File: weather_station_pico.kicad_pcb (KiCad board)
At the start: 2 copper layers, 60.2 x 74.1 mm, 24 parts, among them J1 UART_DEBUG, J2 1984617, J3 STEMMA, J4 STEMMA_QT, J5 DS18B20, J6 1X7_HEADER, J7 RJ11, J8 RJ11, U1 PICO_W, U2 BME280

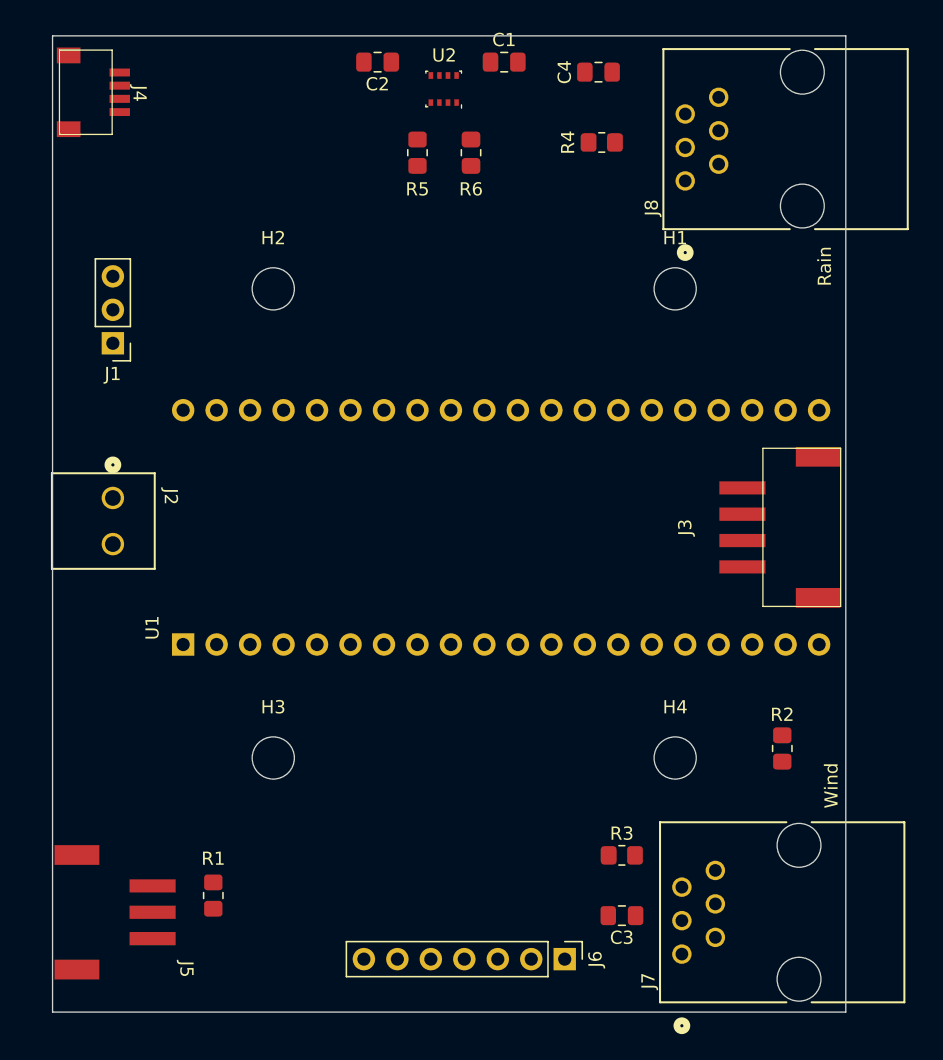
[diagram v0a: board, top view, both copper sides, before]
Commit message: Added footprints for antenna connector
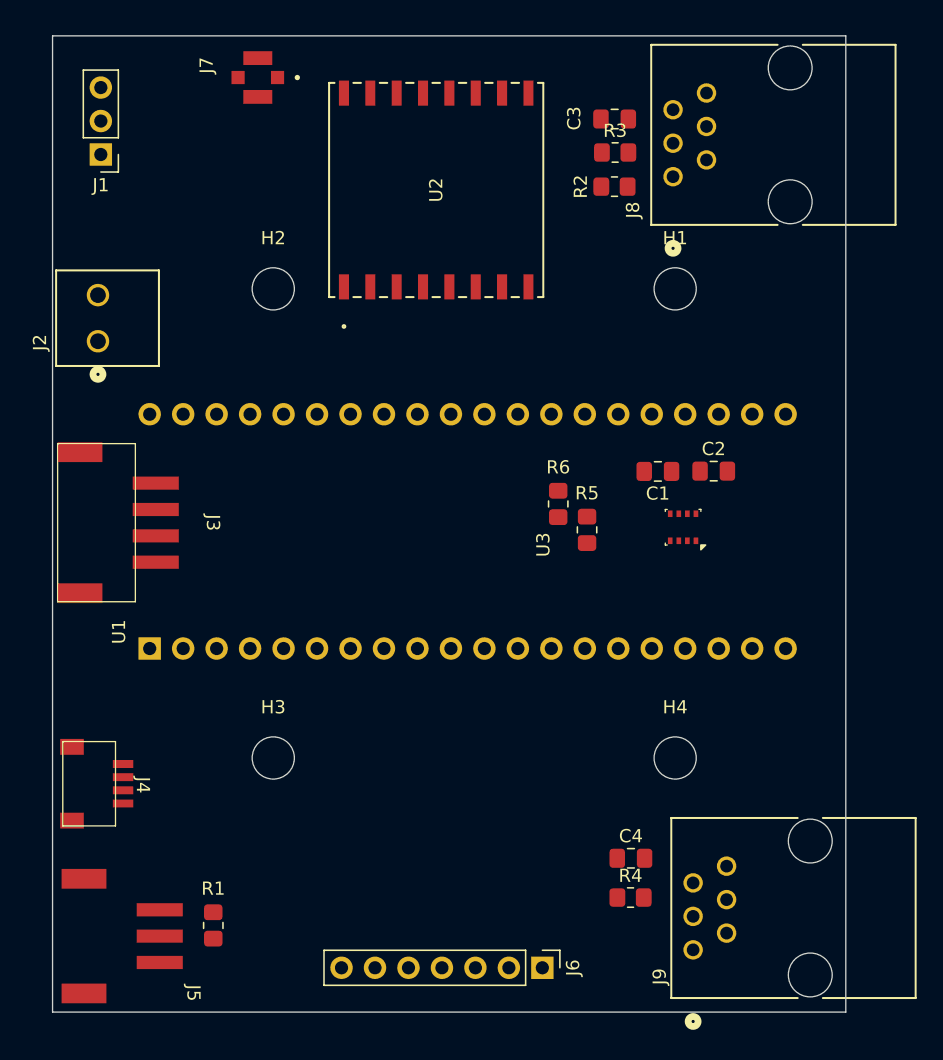
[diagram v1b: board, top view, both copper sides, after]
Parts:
- added J9: RJ11, WeatherStation:CONN6_5555165-1_TEC, F.Cu at (163.4, 114.6)
- added U3: BME280, Package_LGA:Bosch_LGA-8_2.5x2.5mm_P0.65mm_ClockwisePinNumbering, F.Cu at (162.7, 82.5)
- J1: value UART_DEBUG -> Conn_01x03
- J7: value RJ11 -> 73412-0110; footprint WeatherStation:CONN6_5555165-1_TEC -> 734120110:MOLEX_73412-0110
- U1: value PICO_W -> PICO
- U2: value BME280 -> RFM69; footprint Package_LGA:Bosch_LGA-8_2.5x2.5mm_P0.65mm_ClockwisePinNumbering -> RFM69:RFM69HCW_SPK
- moved J7 73.9 mm to (130.4, 48.4)
- moved C3 60.5 mm to (157.5, 51.6)
- moved C4 59.7 mm to (158.7, 107.7), turned to 0 degrees
- moved R4 57.3 mm to (158.7, 110.6)
- moved R3 53.3 mm to (157.5, 54.1)
- moved J4 52.5 mm to (119.4, 102.0)
- moved J3 48.0 mm to (120.9, 82.2), turned to -90 degrees
- moved R2 44.5 mm to (157.4, 56.7), turned to 0 degrees
- moved C2 40.2 mm to (165.0, 78.3), turned to 0 degrees
- moved C1 33.2 mm to (160.7, 78.3), turned to 180 degrees
- moved R5 31.4 mm to (155.4, 82.7), turned to -90 degrees
- moved R6 27.5 mm to (153.2, 80.8), turned to -90 degrees
- moved J1 14.4 mm to (118.5, 54.3)
- moved J2 11.9 mm to (118.2, 68.4), turned to 90 degrees
- moved U2 7.68 mm to (143.9, 56.9), turned to 90 degrees
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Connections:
- J1 pad 1: GND -> /UART_TX
- J1 pad 3: /UART_TX -> GND
- J7 pad 1: unconnected-(J7-Pad1) -> Net-(U2-ANT)
- J7 pad 3: GND -> (no net)
- J7 pad 4: /WINDSPEED_TGR -> (no net)
- J8 pad 2: unconnected-(J8-Pad2) -> GND
- J8 pad 4: /RAIN_COUNT -> /WINDSPEED_TGR
- J8 pad 5: unconnected-(J8-Pad5) -> /WINDDIR_OUT
- U1 pad 21: unconnected-(U1-GP16-Pad21) -> /SPI0_MISO
- U1 pad 22: unconnected-(U1-GP17-Pad22) -> /RFM69_CS
- U1 pad 24: unconnected-(U1-GP18-Pad24) -> /SPI0_CLK
- U1 pad 25: unconnected-(U1-GP19-Pad25) -> /SPI0_MOSI
- U1 pad 26: unconnected-(U1-GP20-Pad26) -> /RFM69_RESET
- U1 pad 27: unconnected-(U1-GP21-Pad27) -> /FRM69_INTR
- U2 pad 2: VCC -> /SPI0_MISO
- U2 pad 3: /SDA -> /SPI0_MOSI
- U2 pad 4: /SCL -> /SPI0_CLK
- U2 pad 5: GND -> /RFM69_CS
- U2 pad 6: VCC -> /RFM69_RESET
- U2 pad 7: GND -> unconnected-(U2-DIO5-Pad7)
- U2 pad 8: VCC -> GND
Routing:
- net VCC: track 1.63 -> 0.00 mm
- net /WINDSPEED_TGR: track 0.59 -> 0.00 mm
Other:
- board text removed: "Rain"
- board text removed: "Wind"
